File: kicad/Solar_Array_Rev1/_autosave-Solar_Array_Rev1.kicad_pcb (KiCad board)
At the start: 2 copper layers, 46 x 30 mm, 34 parts, among them IC1 TVS_4x4, IC2 SPV1040, IC4 TVS_4x4, P1 PV_IN, P2 CONN_01X07, Q1 2N7002WT1GOSCT, Q2 NTR1P02T1GOSCT, Q3 MMBT3904, U1 LTC2990

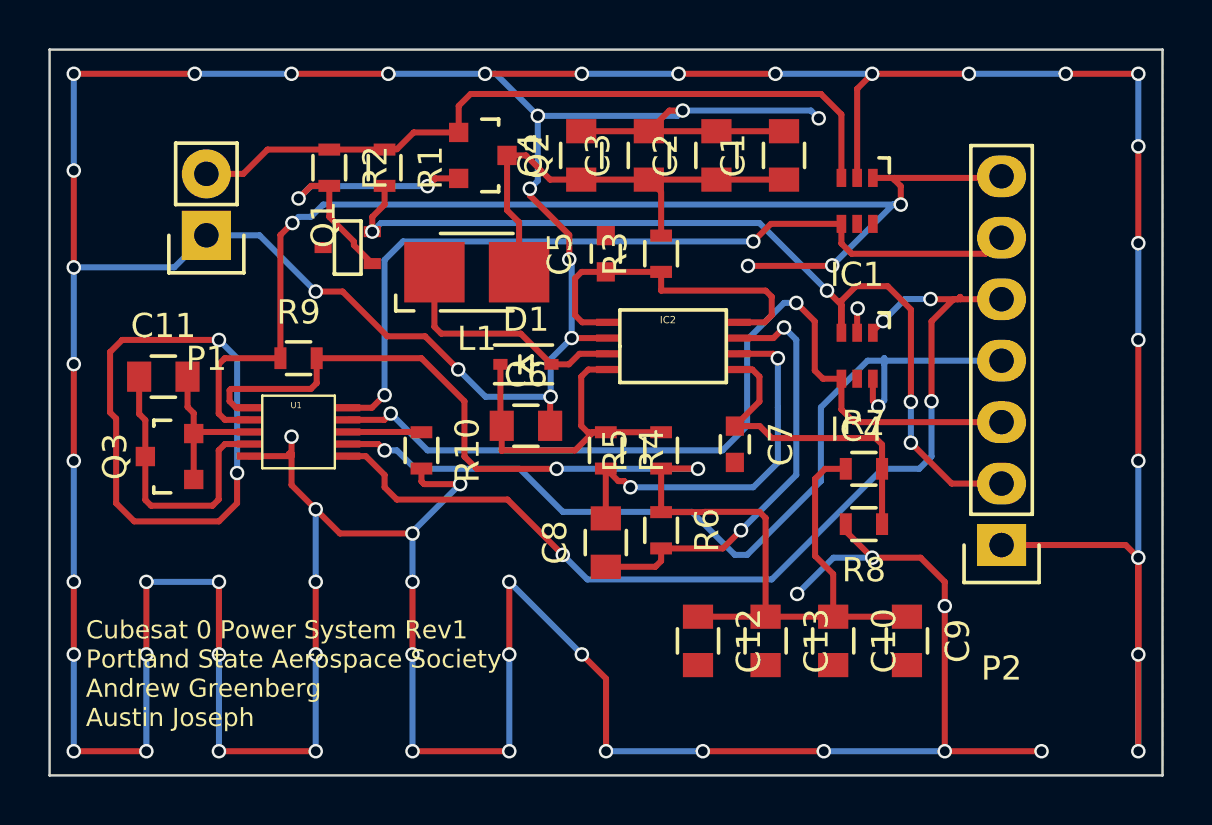
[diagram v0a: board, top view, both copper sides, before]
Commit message: Finished Layout, updated notes, regenerated PDF's -  Finished the board layout with obnoxious stitching. -  Updated component notes for IC's -  Regenerated F/B copper PDF's and schema PDF's
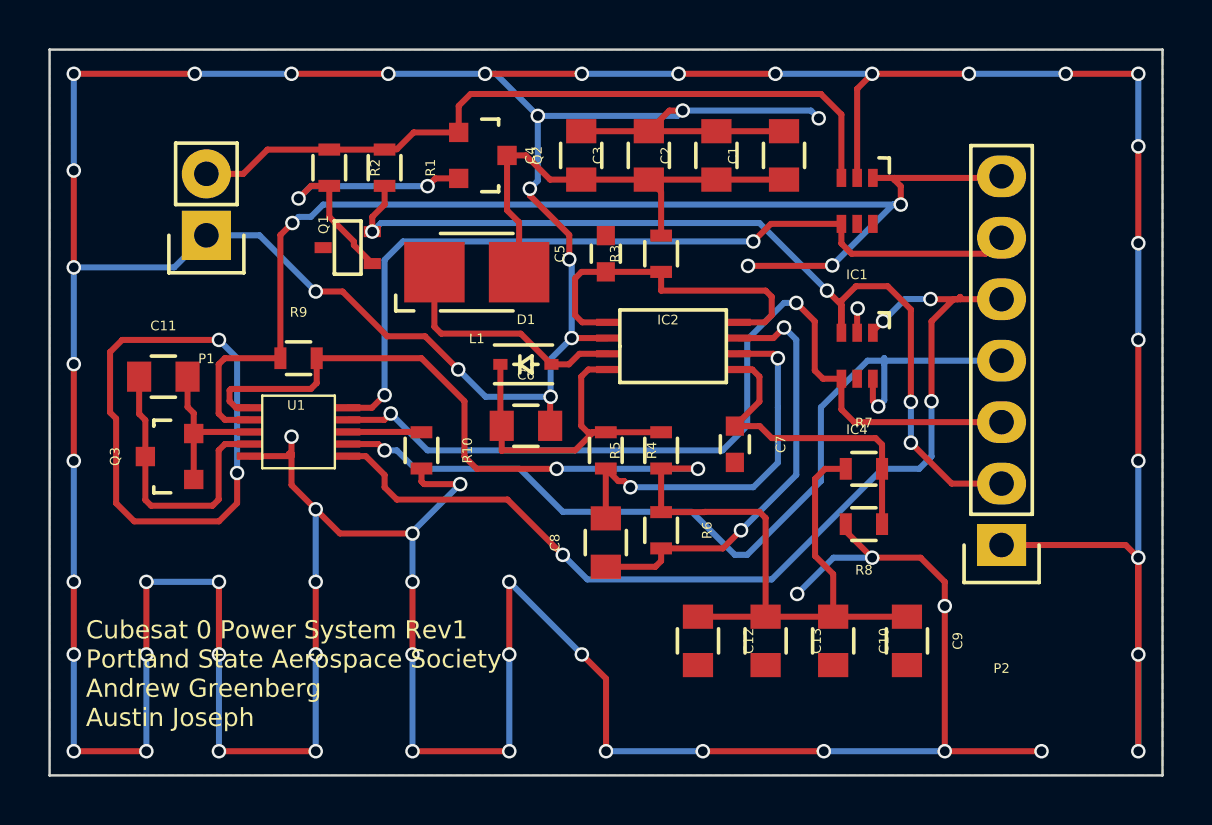
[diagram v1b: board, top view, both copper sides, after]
